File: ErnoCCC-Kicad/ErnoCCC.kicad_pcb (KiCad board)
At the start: 2 copper layers, 161.4 x 95.9 mm, 94 parts, among them J1 6VAC, J2 ICSP, J3 FTDI, J4 Erno Controller, J5 SWITCH, J6 LED OUT, J7 Conn_01x05, Q1 BC847, Q2 BC847, SW1 SW_Push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

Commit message: DRC green!
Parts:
- moved C3 0.14 mm to (209.8, 51.3)
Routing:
- net GND: track 97.1 -> 108.7 mm, vias 7 -> 10
- net Net-(R17-Pad1): track 24.0 -> 34.4 mm
- net +6V: track 147.6 -> 150.4 mm
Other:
- board text added: "D10"
- board text added: "D9"
- board text added: "Gray-A"
- board text added: "Gray-B"
- board text added: "SCL"
- board text added: "SDA"
- board text added: "SSR"

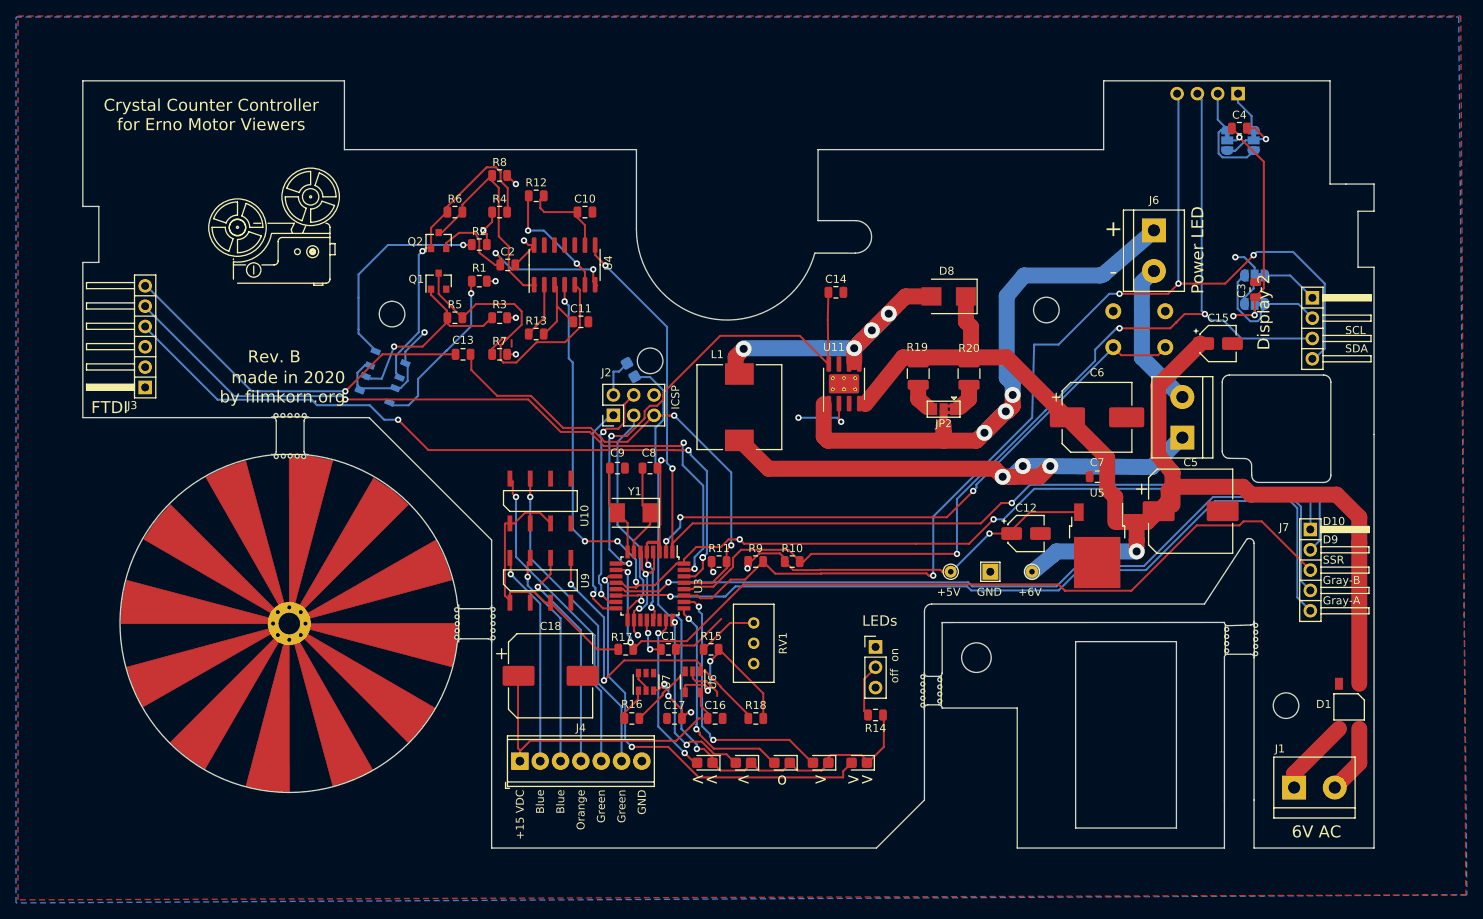
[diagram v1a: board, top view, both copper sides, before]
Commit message: Fixing Encoder Direction, improving Silkscreen
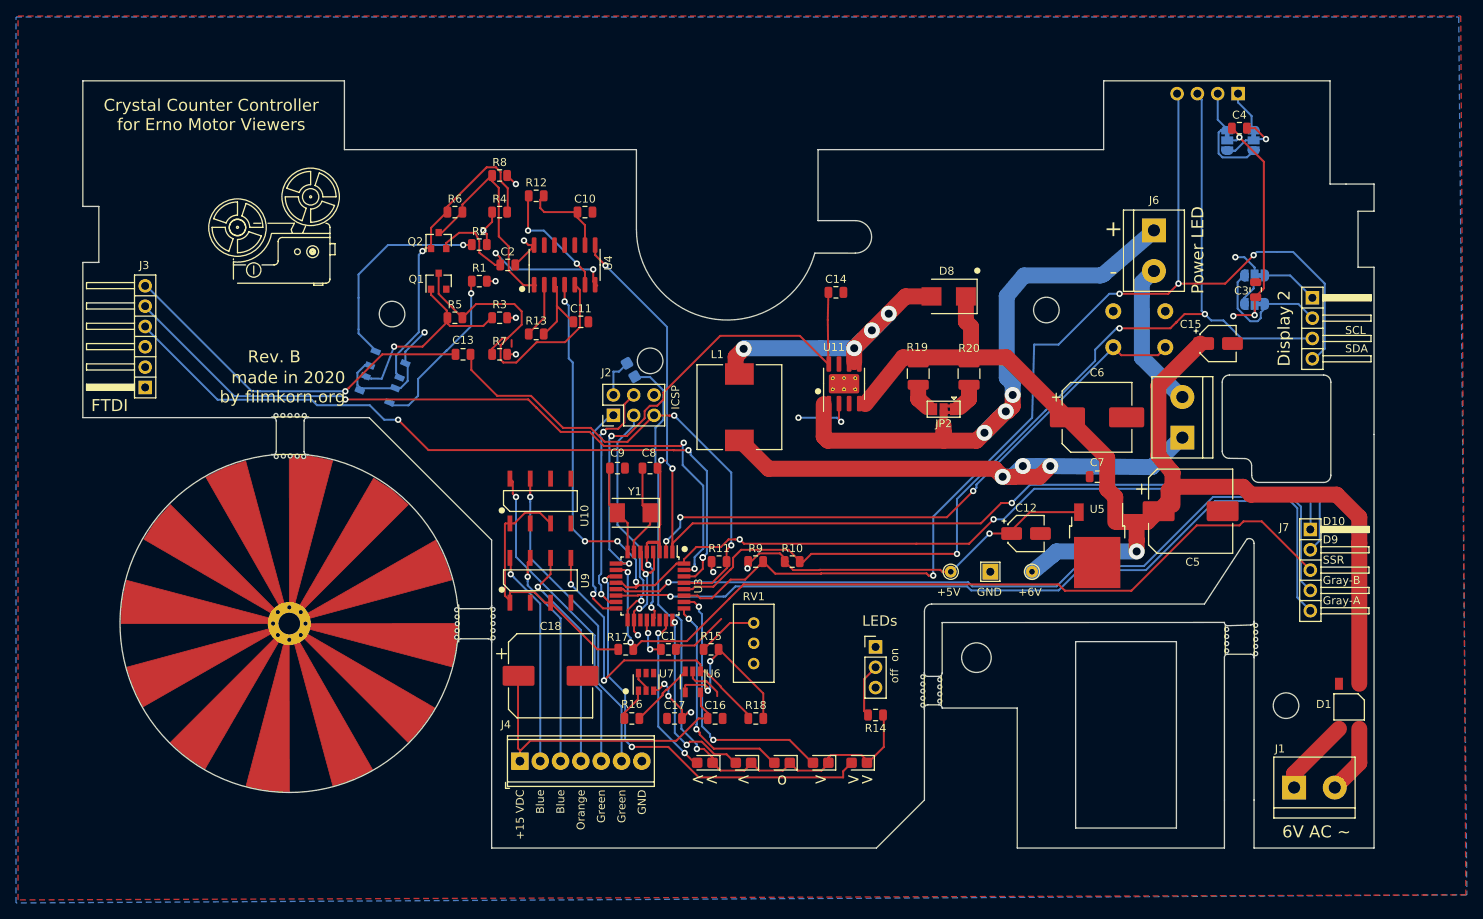
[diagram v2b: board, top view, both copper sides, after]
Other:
- board text added: "6V AC ~~"
- board text added: "•"
- board text removed: "6V AC"
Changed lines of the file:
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@@
   (general
     (thickness 1.6)
-    (drawings 303)
+    (drawings 311)
     (tracks 992)
     (zones 0)
@@
     (descr "Through hole angled pin header, 1x06, 2.54mm pitch, 6mm pin length, single row")
     (tags "Through hole angled pin header THT 1x06 2.54mm single row")
-    (fp_text reference J3 (at 3.7754 -8.62) (layer F.SilkS)
+    (fp_text reference J3 (at 2.286 8.89) (layer F.SilkS)
       (effects (font (size 1 1) (thickness 0.15)))
     )
@@
     (tags "capacitor electrolytic")
     (attr smd)
-    (fp_text reference C15 (at 0 -3.2) (layer F.SilkS)
+    (fp_text reference C15 (at -3.429 -2.413) (layer F.SilkS)
       (effects (font (size 1 1) (thickness 0.15)))
     )
@@
     (tags SOT-23-6)
     (attr smd)
-    (fp_text reference U7 (at 0 2.54 90) (layer F.SilkS)
+    (fp_text reference U7 (at 1.016 2.54 180) (layer F.SilkS)
       (effects (font (size 1 1) (thickness 0.15)))
     )
@@
     (tags TSOT-23-5)
     (attr smd)
-    (fp_text reference U6 (at 0 -2.45 90) (layer F.SilkS)
+    (fp_text reference U6 (at -1.016 -2.54 180) (layer F.SilkS)
       (effects (font (size 1 1) (thickness 0.15)))
     )
@@
     (descr "Potentiometer, vertical, Bourns 3296W, https://www.bourns.com/pdfs/3296.pdf")
     (tags "Potentiometer vertical Bourns 3296W")
-    (fp_text reference RV1 (at -2.54 -3.66 90) (layer F.SilkS)
+    (fp_text reference RV1 (at -8.382 0 180) (layer F.SilkS)
       (effects (font (size 1 1) (thickness 0.15)))
     )
@@
     (descr "Terminal Block Phoenix MPT-0,5-7-2.54, 7 pins, pitch 2.54mm, size 18.2x6.2mm^2, drill diamater 1.1mm, pad diameter 2.2mm, see http://www.mouser.com/ds/2/324/ItemDetail_1725672-916605.pdf, script-generated using https://github.com/pointhi/kicad-footprint-generator/scripts/TerminalBlock_Phoenix")
     (tags "THT Terminal Block Phoenix MPT-0,5-7-2.54 pitch 2.54mm size 18.2x6.2mm^2 drill 1.1mm pad 2.2mm")
-    (fp_text reference J4 (at 7.62 -4.16) (layer F.SilkS)
+    (fp_text reference J4 (at -1.76 -4.572) (layer F.SilkS)
       (effects (font (size 1 1) (thickness 0.15)))
     )
@@
     (tags "DPAK TO-252 DPAK-3 TO-252-3 SOT-428")
     (attr smd)
-    (fp_text reference U5 (at -6.604 0 180) (layer F.SilkS)
+    (fp_text reference U5 (at -4.572 0 180) (layer F.SilkS)
       (effects (font (size 1 1) (thickness 0.15)))
     )
@@
     (tags "capacitor electrolytic")
     (attr smd)
-    (fp_text reference C5 (at 0 -6.096) (layer F.SilkS)
+    (fp_text reference C5 (at 0.254 6.35) (layer F.SilkS)
       (effects (font (size 1 1) (thickness 0.15)))
     )
@@
     (tags capacitor)
     (attr smd)
-    (fp_text reference C3 (at -0.127 -1.778 90) (layer F.SilkS)
+    (fp_text reference C3 (at -0.127 -1.778 180) (layer F.SilkS)
       (effects (font (size 1 1) (thickness 0.15)))
     )
@@
     (tags resistor)
     (attr smd)
-    (fp_text reference R17 (at -0.508 -1.524) (layer F.SilkS)
+    (fp_text reference R17 (at -1.016 -1.524) (layer F.SilkS)
       (effects (font (size 1 1) (thickness 0.15)))
     )
@@
     )
   )
+  (gr_text • (at 115.57 78.994) (layer F.SilkS)
+    (effects (font (size 2 2) (thickness 0.2)))
+  )
+  (gr_text • (at 115.57 88.9) (layer F.SilkS)
+    (effects (font (size 2 2) (thickness 0.2)))
+  )
+  (gr_text • (at 155.194 64.008 90) (layer F.SilkS)
+    (effects (font (size 2 2) (thickness 0.2)))
+  )
+  (gr_text • (at 100.584 66.294) (layer B.SilkS)
+    (effects (font (size 2 2) (thickness 0.2)) (justify mirror))
+  )
+  (gr_text • (at 118.11 51.308) (layer F.SilkS)
+    (effects (font (size 2 2) (thickness 0.2)))
+  )
+  (gr_text • (at 131.064 101.6) (layer F.SilkS)
+    (effects (font (size 2 2) (thickness 0.2)))
+  )
+  (gr_text • (at 138.43 83.82) (layer F.SilkS)
+    (effects (font (size 2 2) (thickness 0.2)))
+  )
+  (gr_text • (at 175.006 49.022) (layer F.SilkS)
+    (effects (font (size 2 2) (thickness 0.2)))
+  )
   (gr_text SCL (at 220.98 56.388) (layer F.SilkS)
     (effects (font (size 1 1) (thickness 0.15)) (justify left))
@@
     (effects (font (size 1.5 1.5) (thickness 0.3)))
   )
-  (gr_text FTDI (at 66.548 66.04) (layer F.SilkS)
+  (gr_text FTDI (at 66.548 65.786) (layer F.SilkS)
     (effects (font (size 1.5 1.5) (thickness 0.3)))
   )
@@
     (effects (font (size 1 1) (thickness 0.15)) (justify right))
   )
-  (gr_text "6V AC" (at 217.406 119.076) (layer F.SilkS)
+  (gr_text "6V AC ~~" (at 217.406 119.076) (layer F.SilkS)
     (effects (font (size 1.5 1.5) (thickness 0.3)))
   )
@@
     (effects (font (size 1.5 1.5) (thickness 0.3)))
   )
-  (gr_text "Display 2" (at 210.82 54.102 90) (layer F.SilkS)
+  (gr_text "Display 2" (at 213.36 56.134 90) (layer F.SilkS)
     (effects (font (size 1.5 1.5) (thickness 0.3)))
   )

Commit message: Ready for Rev.C
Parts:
- added REF**: OSHW-Logo2_7.3x6mm_SilkScreen, Symbol:OSHW-Logo2_7.3x6mm_SilkScreen, F.Cu at (114.8, 66.8)
- added REF**: WEEE-Logo_4.2x6mm_SilkScreen, Symbol:WEEE-Logo_4.2x6mm_SilkScreen, F.Cu at (94.0, 57.4)

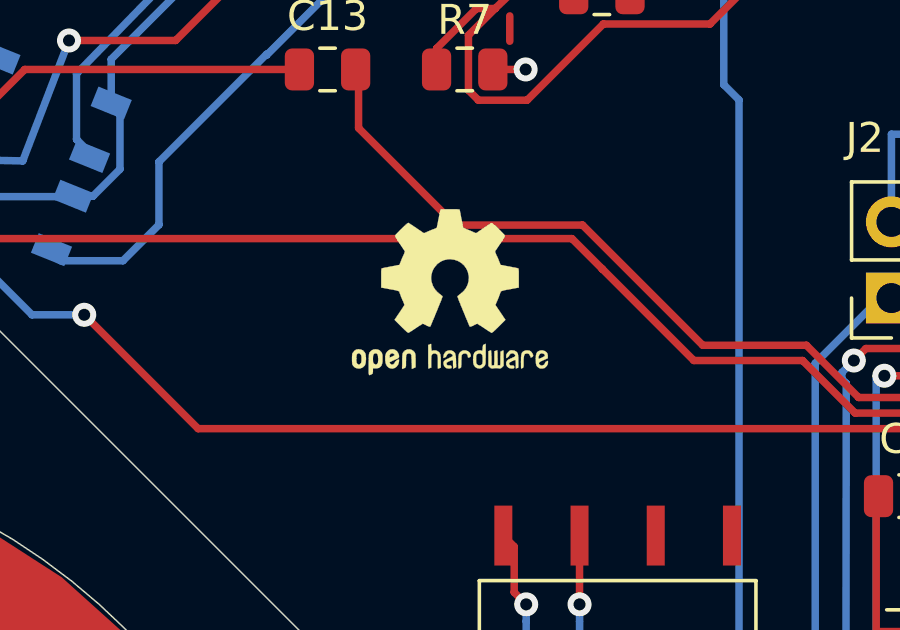
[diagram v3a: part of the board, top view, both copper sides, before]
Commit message: Adding fidicules for the stencil
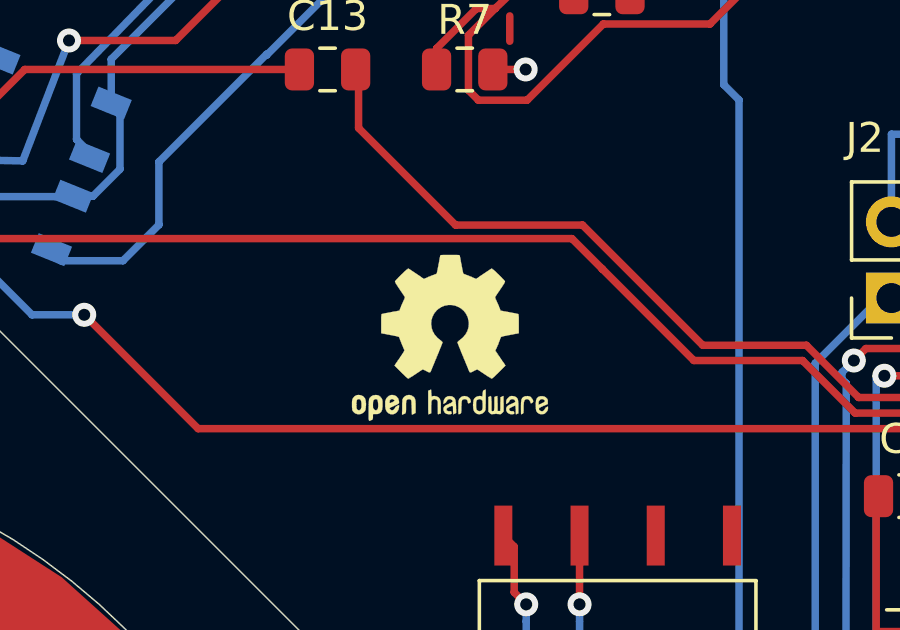
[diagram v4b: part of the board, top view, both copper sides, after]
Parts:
- moved REF** 1.52 mm to (114.8, 68.3)
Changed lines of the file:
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@@
   (general
     (thickness 1.6)
-    (drawings 311)
+    (drawings 313)
     (tracks 992)
     (zones 0)
@@
     (37 F.SilkS user)
     (38 B.Mask user)
-    (39 F.Mask user hide)
+    (39 F.Mask user)
     (40 Dwgs.User user)
     (41 Cmts.User user)
@@
       (drillshape 0)
       (scaleselection 1)
-      (outputdirectory "Gerbers-Rev.A/"))
+      (outputdirectory "Gerbers-Rev.B/"))
   )
   (net 0 "")
@@
   )
   (module Symbol:OSHW-Logo2_7.3x6mm_SilkScreen (layer F.Cu)
-    (at 114.808 66.802)
+    (at 114.808 68.326)
     (descr "Open Source Hardware Symbol")
     (tags "Logo Symbol OSHW")
@@
     )
   )
+  (gr_circle (center 52.2 121.1) (end 55.2 121.1) (layer F.Paste) (width 0.01))
+  (gr_circle (center 52.2 25.2) (end 55.2 25.2) (layer F.Paste) (width 0.01))
   (gr_text • (at 115.57 78.994) (layer F.SilkS)
     (effects (font (size 2 2) (thickness 0.2)))
